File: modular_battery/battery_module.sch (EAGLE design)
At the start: 12 parts

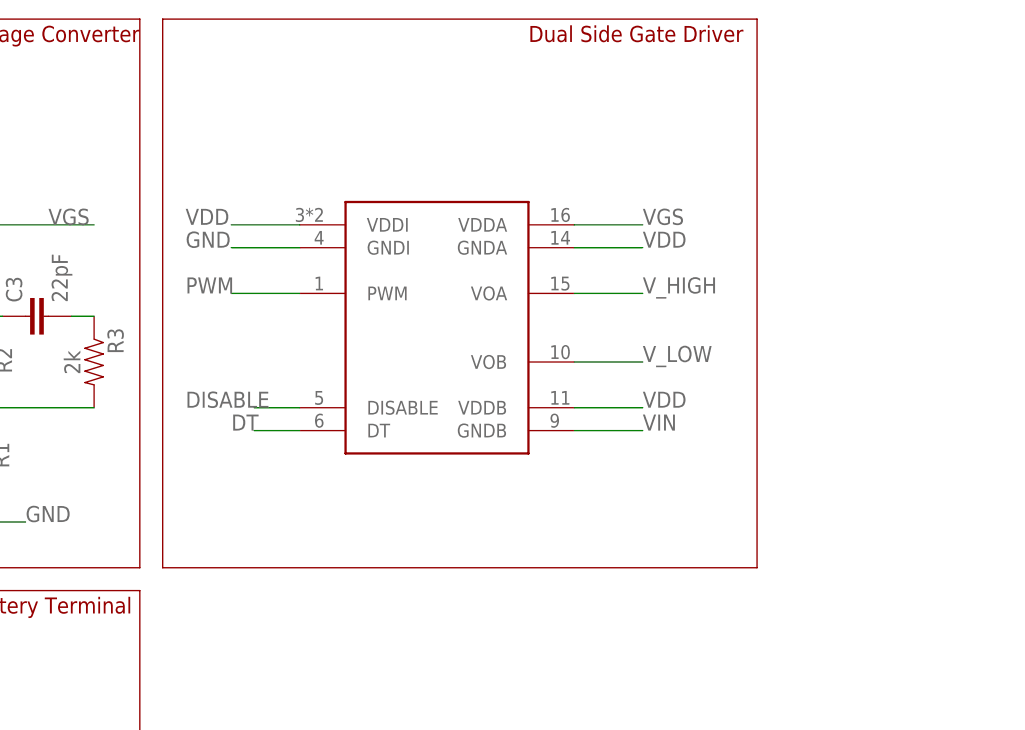
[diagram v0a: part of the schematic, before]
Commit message: Update battery_module.sch
Added bootstrap capacitor to high side mosfet driver.
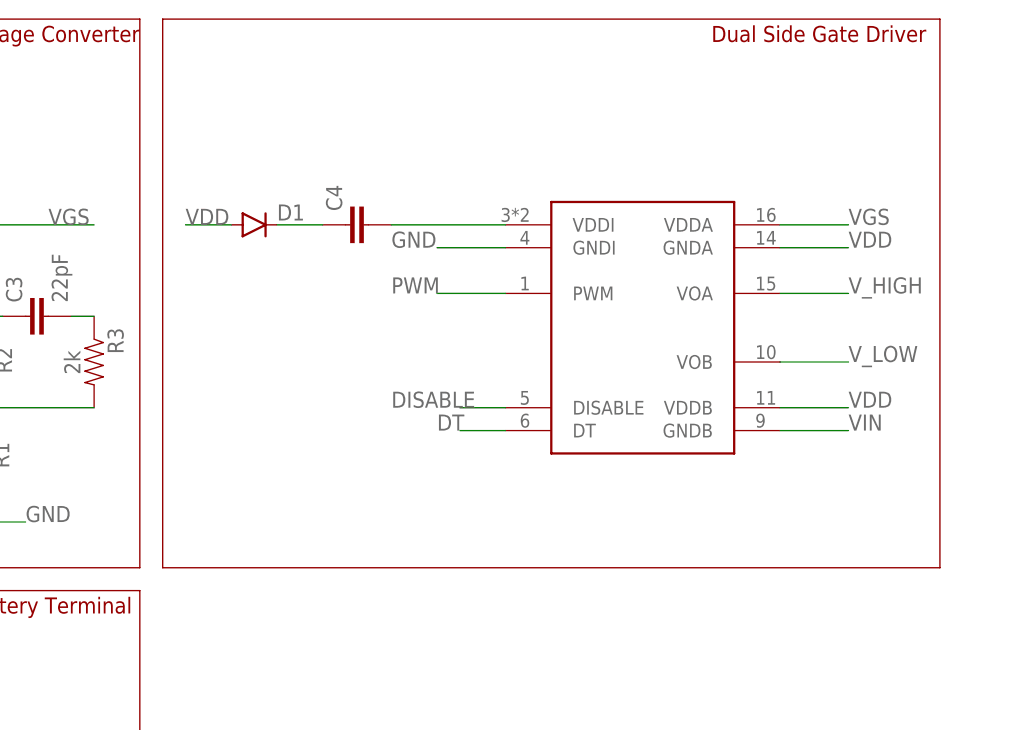
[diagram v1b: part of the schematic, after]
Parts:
- added C4: (no value), SparkFun-Passives:CAP0603-CAP
- added D1: (no value), SparkFun-DiscreteSemi:DIODESMB
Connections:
- new net N$2: C4.1, D1.C
- new net N$4: C4.2, U$4.VDDI
- net VDD: now also D1.A; no longer U$4.VDDI
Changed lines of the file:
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@@
 <part name="HIGH" library="IPT004N03L" deviceset="IPT004N03L" device=""/>
 <part name="L1" library="SparkFun-Passives" deviceset="INDUCTOR" device="30OHM,1.8A" value="22uH"/>
+<part name="C4" library="SparkFun-Passives" deviceset="CAP" device="0603-CAP"/>
+<part name="D1" library="SparkFun-DiscreteSemi" deviceset="DIODE" device="SMB"/>
 </parts>
 <sheets>
@@
 <wire x1="-25.4" y1="0" x2="-25.4" y2="43.18" width="0.1524" layer="94"/>
 <text x="12.7" y="40.64" size="1.778" layer="94">S1 Battery Terminal</text>
-<text x="78.74" y="104.14" size="1.778" layer="94">Dual Side Gate Driver</text>
-<wire x1="38.1" y1="106.68" x2="104.14" y2="106.68" width="0.1524" layer="94"/>
-<wire x1="104.14" y1="106.68" x2="104.14" y2="45.72" width="0.1524" layer="94"/>
-<wire x1="104.14" y1="45.72" x2="38.1" y2="45.72" width="0.1524" layer="94"/>
+<text x="99.06" y="104.14" size="1.778" layer="94">Dual Side Gate Driver</text>
+<wire x1="38.1" y1="106.68" x2="124.46" y2="106.68" width="0.1524" layer="94"/>
+<wire x1="124.46" y1="106.68" x2="124.46" y2="45.72" width="0.1524" layer="94"/>
+<wire x1="124.46" y1="45.72" x2="38.1" y2="45.72" width="0.1524" layer="94"/>
 <wire x1="38.1" y1="45.72" x2="38.1" y2="106.68" width="0.1524" layer="94"/>
 <text x="53.34" y="20.32" size="3.556" layer="94">LiPO Battery Module</text>
@@
 <instances>
 <instance part="U$3" gate="G$1" x="15.24" y="17.78"/>
-<instance part="U$4" gate="G$1" x="68.58" y="78.74"/>
+<instance part="U$4" gate="G$1" x="91.44" y="78.74"/>
 <instance part="LOW" gate="G$1" x="-2.54" y="12.7">
 <attribute name="NAME" x="-3.81" y="13.97" size="1.27" layer="95"/>
@@
 <attribute name="NAME" x="-17.78" y="73.66" size="1.778" layer="95" rot="R180"/>
 <attribute name="VALUE" x="-17.78" y="83.82" size="1.778" layer="96" rot="R180"/>
+</instance>
+<instance part="C4" gate="G$1" x="60.96" y="83.82" rot="R90">
+<attribute name="NAME" x="58.039" y="85.344" size="1.778" layer="95" rot="R90"/>
+<attribute name="VALUE" x="63.119" y="85.344" size="1.778" layer="96" rot="R90"/>
+</instance>
+<instance part="D1" gate="G$1" x="48.26" y="83.82">
+<attribute name="NAME" x="50.8" y="84.3026" size="1.778" layer="95"/>
+<attribute name="VALUE" x="50.8" y="81.5086" size="1.778" layer="96"/>
 </instance>
 </instances>
@@
 <segment>
 <pinref part="U$4" gate="G$1" pin="GNDI"/>
-<wire x1="53.34" y1="81.28" x2="45.72" y2="81.28" width="0.1524" layer="91"/>
-<label x="40.64" y="81.28" size="1.778" layer="95"/>
+<wire x1="76.2" y1="81.28" x2="68.58" y2="81.28" width="0.1524" layer="91"/>
+<label x="63.5" y="81.28" size="1.778" layer="95"/>
 </segment>
 </net>
@@
 <segment>
 <pinref part="U$4" gate="G$1" pin="VDDB"/>
-<wire x1="83.82" y1="63.5" x2="91.44" y2="63.5" width="0.1524" layer="91"/>
-<label x="91.44" y="63.5" size="1.778" layer="95"/>
+<wire x1="106.68" y1="63.5" x2="114.3" y2="63.5" width="0.1524" layer="91"/>
+<label x="114.3" y="63.5" size="1.778" layer="95"/>
 </segment>
 <segment>
 <pinref part="U$4" gate="G$1" pin="GNDA"/>
-<wire x1="83.82" y1="81.28" x2="91.44" y2="81.28" width="0.1524" layer="91"/>
-<label x="91.44" y="81.28" size="1.778" layer="95"/>
-</segment>
-<segment>
-<pinref part="U$4" gate="G$1" pin="VDDI"/>
-<wire x1="53.34" y1="83.82" x2="45.72" y2="83.82" width="0.1524" layer="91"/>
+<wire x1="106.68" y1="81.28" x2="114.3" y2="81.28" width="0.1524" layer="91"/>
+<label x="114.3" y="81.28" size="1.778" layer="95"/>
+</segment>
+<segment>
+<pinref part="D1" gate="G$1" pin="A"/>
+<wire x1="45.72" y1="83.82" x2="40.64" y2="83.82" width="0.1524" layer="91"/>
 <label x="40.64" y="83.82" size="1.778" layer="95"/>
 </segment>
@@
 <segment>
 <pinref part="U$4" gate="G$1" pin="VDDA"/>
-<wire x1="83.82" y1="83.82" x2="91.44" y2="83.82" width="0.1524" layer="91"/>
-<label x="91.44" y="83.82" size="1.778" layer="95"/>
+<wire x1="106.68" y1="83.82" x2="114.3" y2="83.82" width="0.1524" layer="91"/>
+<label x="114.3" y="83.82" size="1.778" layer="95"/>
 </segment>
 </net>
@@
 <segment>
 <pinref part="U$4" gate="G$1" pin="VOB"/>
-<wire x1="83.82" y1="68.58" x2="91.44" y2="68.58" width="0.1524" layer="91"/>
-<label x="91.44" y="68.58" size="1.778" layer="95"/>
+<wire x1="106.68" y1="68.58" x2="114.3" y2="68.58" width="0.1524" layer="91"/>
+<label x="114.3" y="68.58" size="1.778" layer="95"/>
 </segment>
 </net>
@@
 <segment>
 <pinref part="U$4" gate="G$1" pin="VOA"/>
-<wire x1="83.82" y1="76.2" x2="91.44" y2="76.2" width="0.1524" layer="91"/>
-<label x="91.44" y="76.2" size="1.778" layer="95"/>
+<wire x1="106.68" y1="76.2" x2="114.3" y2="76.2" width="0.1524" layer="91"/>
+<label x="114.3" y="76.2" size="1.778" layer="95"/>
 </segment>
 </net>
@@
 <segment>
 <pinref part="U$4" gate="G$1" pin="GNDB"/>
-<wire x1="83.82" y1="60.96" x2="91.44" y2="60.96" width="0.1524" layer="91"/>
-<label x="91.44" y="60.96" size="1.778" layer="95"/>
+<wire x1="106.68" y1="60.96" x2="114.3" y2="60.96" width="0.1524" layer="91"/>
+<label x="114.3" y="60.96" size="1.778" layer="95"/>
 </segment>
 </net>
@@
 <segment>
 <pinref part="U$4" gate="G$1" pin="PWM"/>
-<wire x1="53.34" y1="76.2" x2="45.72" y2="76.2" width="0.1524" layer="91"/>
-<label x="40.64" y="76.2" size="1.778" layer="95"/>
+<wire x1="76.2" y1="76.2" x2="68.58" y2="76.2" width="0.1524" layer="91"/>
+<label x="63.5" y="76.2" size="1.778" layer="95"/>
 </segment>
 </net>
@@
 <segment>
 <pinref part="U$4" gate="G$1" pin="DISABLE"/>
-<wire x1="53.34" y1="63.5" x2="48.26" y2="63.5" width="0.1524" layer="91"/>
-<label x="40.64" y="63.5" size="1.778" layer="95"/>
+<wire x1="76.2" y1="63.5" x2="71.12" y2="63.5" width="0.1524" layer="91"/>
+<label x="63.5" y="63.5" size="1.778" layer="95"/>
 </segment>
 </net>
@@
 <segment>
 <pinref part="U$4" gate="G$1" pin="DT"/>
-<wire x1="53.34" y1="60.96" x2="48.26" y2="60.96" width="0.1524" layer="91"/>
-<label x="45.72" y="60.96" size="1.778" layer="95"/>
-</segment>
-</net>
+<wire x1="76.2" y1="60.96" x2="71.12" y2="60.96" width="0.1524" layer="91"/>
+<label x="68.58" y="60.96" size="1.778" layer="95"/>
+</segment>
+</net>
+<net name="N$2" class="0">
+<segment>
+<pinref part="D1" gate="G$1" pin="C"/>
+<pinref part="C4" gate="G$1" pin="1"/>
+<wire x1="50.8" y1="83.82" x2="55.88" y2="83.82" width="0.1524" layer="91"/>
+</segment>
+</net>
+<net name="N$4" class="0">
+<segment>
+<pinref part="C4" gate="G$1" pin="2"/>
+<pinref part="U$4" gate="G$1" pin="VDDI"/>
+<wire x1="63.5" y1="83.82" x2="76.2" y2="83.82" width="0.1524" layer="91"/>
+</segment>
+</net>

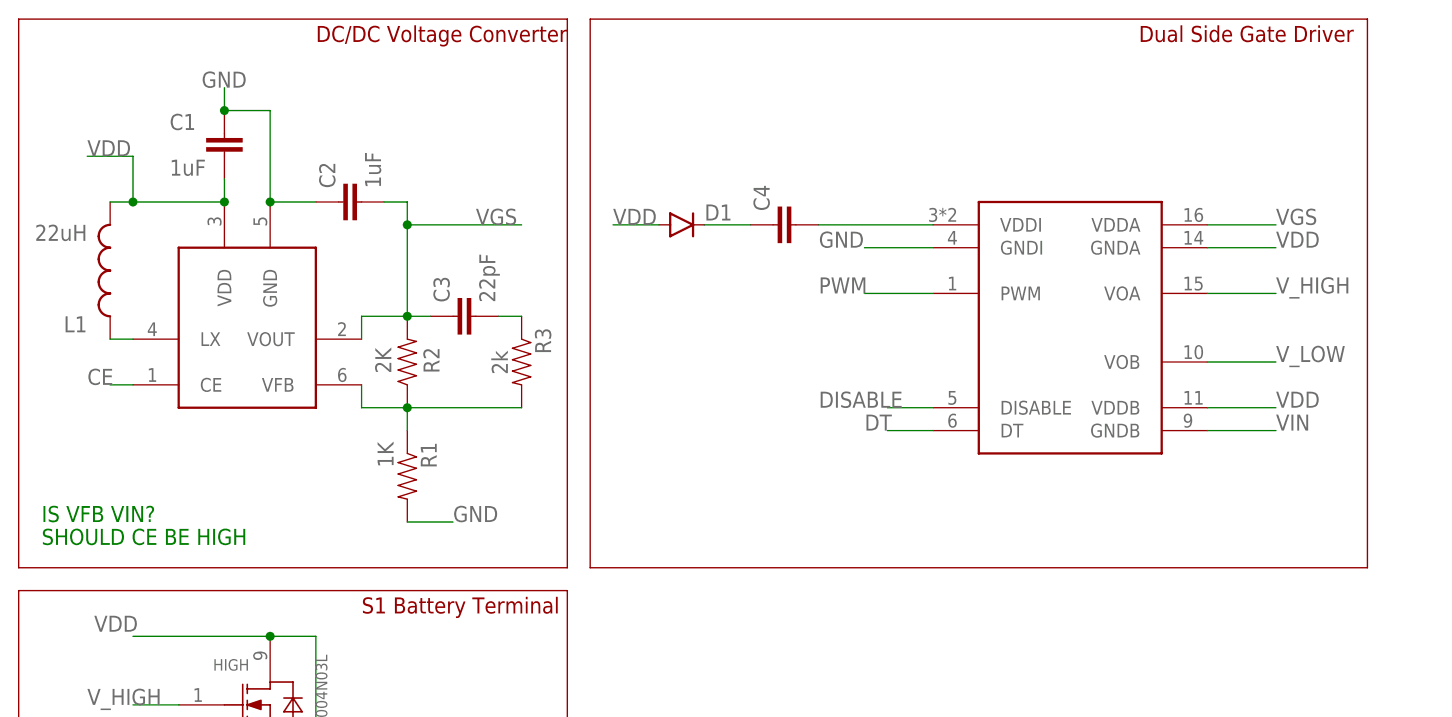
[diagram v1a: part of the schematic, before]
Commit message: boot strap and boost converter fixes
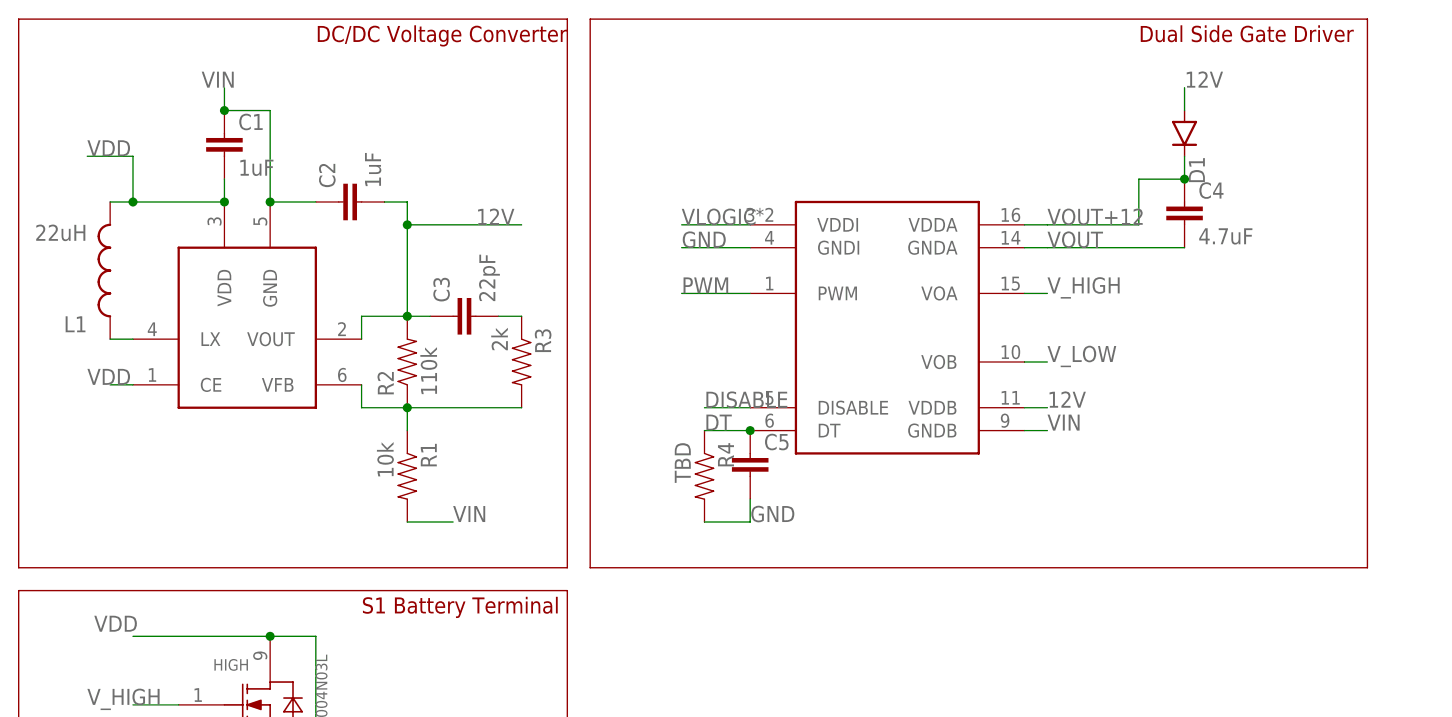
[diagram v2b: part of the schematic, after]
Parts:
- added C5: (no value), SparkFun-Passives:CAP0603-CAP
- added R4: TBD, SparkFun-Resistors:RESISTOR0603
- C4: value (none) -> 4.7uF
- R1: value 1K -> 10k
- R2: value 2K -> 110k
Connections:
- removed net CE: R1200.CE
- removed net N$2: C4.1, D1.C
- removed net N$4: C4.2, U$4.VDDI
- removed net VGS: C2.2, C3.1, R1200.VOUT, R2.2, U$4.VDDA
- new net 12V: C2.2, C3.1, D1.A, R1200.VOUT, R2.2, U$4.VDDB
- new net VLOGIC: U$4.VDDI
- new net VOUT+12: C4.1, D1.C, U$4.VDDA
- net DT: now also C5.1, R4.1
- net GND: now also C5.2, R4.2; no longer C1.1, C2.1, R1.2, R1200.GND
- net VDD: now also R1200.CE; no longer D1.A, U$4.GNDA, U$4.VDDB
- net VIN: now also C1.1, C2.1, R1.2, R1200.GND
- net VOUT: now also C4.2, U$4.GNDA
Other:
- note removed: "IS VFB VIN?"
- note removed: "SHOULD CE BE HIGH"
- moved on the sheet: C4, D1

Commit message: Layout for Modular Battery
Updated schematic for individual battery module and began layout for eight cell modular battery.
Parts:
- added ARRAY1: 47k, Custom_old:EXB-2HV
- added C10, C15, C20, C25, C30, C35, C40: (no value), SparkFun-Passives:CAP0603-CAP
- added C11, C13, C16, C18, C21, C23, C26, C28, C31, C33, C36, C38, C6, C8: 1uF, SparkFun-Capacitors:CAP0603-CAP
- added C12, C17, C22, C27, C32, C37, C7: 22pF, SparkFun-Capacitors:CAP0603-CAP
- added C14, C19, C24, C29, C34, C39, C9: 4.7uF, SparkFun-Passives:CAP0603-CAP
- added D2, D3, D4, D5, D6, D7, D8: (no value), SparkFun-DiscreteSemi:DIODESMB
- added HIGH1, HIGH2, HIGH3, HIGH4, HIGH5, HIGH6, HIGH7, LOW1, LOW2, LOW3, LOW4, LOW5, LOW6, LOW7: IPT004N03L, IPT004N03L:IPT004N03L
- added L2, L3, L4, L5, L6, L7, L8: (no value), PowerMagnetics (rev18e):WE-LQS_4025_74404043220A
- added R10, R15, R20, R25, R30, R35, R5: 10k, SparkFun-Resistors:RESISTOR0603
- added R11, R16, R21, R26, R31, R36, R6: 110k, SparkFun-Resistors:RESISTOR0603
- added R12, R17, R22, R27, R32, R37, R7: 2k, SparkFun-Resistors:RESISTOR0603
- added R13, R18, R23, R28, R33, R38, R8: R1200SOT-23-6, Custom_old:R1200SOT-23-6
- added R14, R19, R24, R29, R34, R39, R9: TBD, SparkFun-Resistors:RESISTOR0603
- added RC1_1, RC1_2, RC1_3, RC1_4, RC2_1, RC2_2, RC2_3, RC2_4: (no value), SparkFun-Capacitors:CAP1206
- added SI1, SI2, SI3, SI4, SI5, SI6, SI7, SI823: SI8231SOIC16W, Custom_old:SI8231SOIC16W
- added U$1, U$11: EXB-2HV, Custom_old:EXB-2HV
- added U$10, U$12: LM324, Custom_old:LM324
- added U$2, U$5, U$6, U$7, U$8, U$9: HEADER2, Custom_old:HEADER2
- L1: value 22uH -> (none); device SparkFun-Passives:INDUCTOR30OHM,1.8A -> PowerMagnetics (rev18e):WE-LQS_4025_74404043220A
- U$4: value SI8231SOIC16W -> HEADER2; device Custom_old:SI8231SOIC16W -> Custom_old:HEADER2
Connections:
- removed net 12V: C2.2, C3.1, D1.A, R1200.VOUT, R2.2, U$4.VDDB
- removed net DISABLE: U$4.DISABLE
- removed net DT: C5.1, R4.1, U$4.DT
- removed net PWM: U$4.PWM
- removed net VDD: C1.2, HIGH.9, L1.2, R1200.CE, R1200.VDD, U$3.1
- removed net VIN: C1.1, C2.1, LOW.2, LOW.3, LOW.4, LOW.5, LOW.6, LOW.7, LOW.8, R1.2, R1200.GND, U$3.2, U$4.GNDB
- removed net VOUT: C4.2, HIGH.2, HIGH.3, HIGH.4, HIGH.5, HIGH.6, HIGH.7, HIGH.8, LOW.9, U$4.GNDA
- removed net VOUT+12: C4.1, D1.C, U$4.VDDA
- removed net V_HIGH: HIGH.1, U$4.VOA
- removed net V_LOW: LOW.1, U$4.VOB
- new net 12V_A: C2.2, C3.1, D1.A, R1200.VOUT, R2.2, SI823.VDDB
- new net 12V_B: C7.1, C8.2, D2.A, R6.2, R8.VOUT, SI1.VDDB
- new net 12V_C: C12.1, C13.2, D3.A, R11.2, R13.VOUT, SI2.VDDB
- new net 12V_D: C17.1, C18.2, D4.A, R16.2, R18.VOUT, SI3.VDDB
- new net 12V_E: C22.1, C23.2, D5.A, R21.2, R23.VOUT, SI4.VDDB
- new net 12V_F: C27.1, C28.2, D6.A, R26.2, R28.VOUT, SI5.VDDB
- new net 12V_G: C32.1, C33.2, D7.A, R31.2, R33.VOUT, SI6.VDDB
- new net 12V_H: C37.1, C38.2, D8.A, R36.2, R38.VOUT, SI7.VDDB
- new net DISABLE_A: SI823.DISABLE
- new net DISABLE_B: SI1.DISABLE
- new net DISABLE_C: SI2.DISABLE
- new net DISABLE_D: SI3.DISABLE
- new net DISABLE_E: SI4.DISABLE
- new net DISABLE_F: SI5.DISABLE
- new net DISABLE_G: SI6.DISABLE
- new net DISABLE_H: SI7.DISABLE
- new net DT_A: C5.1, R4.1, SI823.DT
- new net DT_B: C10.1, R9.1, SI1.DT
- new net DT_C: C15.1, R14.1, SI2.DT
- new net DT_D: C20.1, R19.1, SI3.DT
- new net DT_E: C25.1, R24.1, SI4.DT
- new net DT_F: C30.1, R29.1, SI5.DT
- new net DT_G: C35.1, R34.1, SI6.DT
- new net DT_H: C40.1, R39.1, SI7.DT
- new net N$10: R15.1, R16.1, R17.2, R18.VFB
- new net N$11: L4.1, R18.LX
- new net N$12: C17.2, R17.1
- new net N$13: R20.1, R21.1, R22.2, R23.VFB
- new net N$14: L5.1, R23.LX
- new net N$15: C22.2, R22.1
- new net N$16: R25.1, R26.1, R27.2, R28.VFB
- new net N$17: L6.1, R28.LX
- new net N$18: C27.2, R27.1
- new net N$19: R30.1, R31.1, R32.2, R33.VFB
- new net N$2: R5.1, R6.1, R7.2, R8.VFB
- new net N$20: L7.1, R33.LX
- new net N$21: C32.2, R32.1
- new net N$22: R35.1, R36.1, R37.2, R38.VFB
- new net N$23: L8.1, R38.LX
- new net N$24: C37.2, R37.1
- new net N$4: L2.1, R8.LX
- new net N$6: C7.2, R7.1
- new net N$7: R10.1, R11.1, R12.2, R13.VFB
- new net N$8: L3.1, R13.LX
- new net N$9: C12.2, R12.1
- new net PWM_A: SI823.PWM
- new net PWM_B: SI1.PWM
- new net PWM_C: SI2.PWM
- new net PWM_D: SI3.PWM
- new net PWM_E: SI4.PWM
- new net PWM_F: SI5.PWM
- new net PWM_G: SI6.PWM
- new net PWM_H: SI7.PWM
- new net VDD_A: ARRAY1.P$1, C1.2, HIGH.9, L1.2, R1200.CE, R1200.VDD, U$3.1
- new net VDD_B: ARRAY1.P$2, C6.2, HIGH1.9, L2.2, R8.CE, R8.VDD, U$2.1
- new net VDD_C: ARRAY1.P$3, C11.2, HIGH2.9, L3.2, R13.CE, R13.VDD, U$4.1
- new net VDD_D: ARRAY1.P$4, C16.2, HIGH3.9, L4.2, R18.CE, R18.VDD, U$5.1
- new net VDD_E: ARRAY1.P$5, C21.2, HIGH4.9, L5.2, R23.CE, R23.VDD, U$6.1
- new net VDD_F: ARRAY1.P$6, C26.2, HIGH5.9, L6.2, R28.CE, R28.VDD, U$7.1
- new net VDD_G: ARRAY1.P$7, C31.2, HIGH6.9, L7.2, R33.CE, R33.VDD, U$8.1
- new net VDD_H: ARRAY1.P$8, C36.2, HIGH7.9, L8.2, R38.CE, R38.VDD, U$9.1
- new net VDIVRC_A: RC1_1.1, U$11.P$16, U$12.1IN+
- new net VDIVRC_B: RC1_2.1, U$11.P$15, U$12.2IN+
- new net VDIVRC_C: RC1_3.1, U$11.P$14, U$12.3IN+
- new net VDIVRC_D: RC1_4.1, U$11.P$13, U$12.4IN+
- new net VDIVRC_E: RC2_1.1, U$10.1IN+, U$10.2IN+, U$11.P$12
- new net VDIVRC_F: RC2_2.1, U$11.P$11
- new net VDIVRC_G: RC2_3.1, U$10.3IN+, U$11.P$10
- new net VDIVRC_H: RC2_4.1, U$10.4IN+, U$11.P$9
- new net VDIV_A: ARRAY1.P$16, U$1.P$1, U$11.P$1
- new net VDIV_B: ARRAY1.P$15, U$1.P$2, U$11.P$2
- new net VDIV_C: ARRAY1.P$14, U$1.P$3, U$11.P$3
- new net VDIV_D: ARRAY1.P$13, U$1.P$4, U$11.P$4
- new net VDIV_E: ARRAY1.P$12, U$1.P$5, U$11.P$5
- new net VDIV_F: ARRAY1.P$11, U$1.P$6, U$11.P$6
- new net VDIV_G: ARRAY1.P$10, U$1.P$7, U$11.P$7
- new net VDIV_H: ARRAY1.P$9, U$1.P$8, U$11.P$8
- new net VIN_A: C1.1, C2.1, LOW.2, LOW.3, LOW.4, LOW.5, LOW.6, LOW.7, LOW.8, R1.2, R1200.GND, SI823.GNDB, U$3.2
- new net VOUT+12_A: C4.1, D1.C, SI823.VDDA
- new net VOUT+12_B: C9.1, D2.C, SI1.VDDA
- new net VOUT+12_C: C14.1, D3.C, SI2.VDDA
- new net VOUT+12_D: C19.1, D4.C, SI3.VDDA
- new net VOUT+12_E: C24.1, D5.C, SI4.VDDA
- new net VOUT+12_F: C29.1, D6.C, SI5.VDDA
- new net VOUT+12_G: C34.1, D7.C, SI6.VDDA
- new net VOUT+12_H: C39.1, D8.C, SI7.VDDA
- new net VOUT_A: C4.2, C6.1, C8.1, HIGH.2, HIGH.3, HIGH.4, HIGH.5, HIGH.6, HIGH.7, HIGH.8, LOW.9, LOW1.2, LOW1.3, LOW1.4, LOW1.5, LOW1.6, LOW1.7, LOW1.8, R5.2, R8.GND, SI1.GNDB, SI823.GNDA, U$2.2
- new net VOUT_B: C11.1, C13.1, C9.2, HIGH1.2, HIGH1.3, HIGH1.4, HIGH1.5, HIGH1.6, HIGH1.7, HIGH1.8, LOW1.9, LOW2.2, LOW2.3, LOW2.4, LOW2.5, LOW2.6, LOW2.7, LOW2.8, R10.2, R13.GND, SI1.GNDA, SI2.GNDB, U$4.2
- new net VOUT_C: C14.2, C16.1, C18.1, HIGH2.2, HIGH2.3, HIGH2.4, HIGH2.5, HIGH2.6, HIGH2.7, HIGH2.8, LOW2.9, LOW3.2, LOW3.3, LOW3.4, LOW3.5, LOW3.6, LOW3.7, LOW3.8, R15.2, R18.GND, SI2.GNDA, SI3.GNDB, U$5.2
- new net VOUT_D: C19.2, C21.1, C23.1, HIGH3.2, HIGH3.3, HIGH3.4, HIGH3.5, HIGH3.6, HIGH3.7, HIGH3.8, LOW3.9, LOW4.2, LOW4.3, LOW4.4, LOW4.5, LOW4.6, LOW4.7, LOW4.8, R20.2, R23.GND, SI3.GNDA, SI4.GNDB, U$6.2
- new net VOUT_E: C24.2, C26.1, C28.1, HIGH4.2, HIGH4.3, HIGH4.4, HIGH4.5, HIGH4.6, HIGH4.7, HIGH4.8, LOW4.9, LOW5.2, LOW5.3, LOW5.4, LOW5.5, LOW5.6, LOW5.7, LOW5.8, R25.2, R28.GND, SI4.GNDA, SI5.GNDB, U$7.2
- new net VOUT_F: C29.2, C31.1, C33.1, HIGH5.2, HIGH5.3, HIGH5.4, HIGH5.5, HIGH5.6, HIGH5.7, HIGH5.8, LOW5.9, LOW6.2, LOW6.3, LOW6.4, LOW6.5, LOW6.6, LOW6.7, LOW6.8, R30.2, R33.GND, SI5.GNDA, SI6.GNDB, U$8.2
- new net VOUT_G: C34.2, C36.1, C38.1, HIGH6.2, HIGH6.3, HIGH6.4, HIGH6.5, HIGH6.6, HIGH6.7, HIGH6.8, LOW6.9, LOW7.2, LOW7.3, LOW7.4, LOW7.5, LOW7.6, LOW7.7, LOW7.8, R35.2, R38.GND, SI6.GNDA, SI7.GNDB, U$9.2
- new net VOUT_H: C39.2, HIGH7.2, HIGH7.3, HIGH7.4, HIGH7.5, HIGH7.6, HIGH7.7, HIGH7.8, LOW7.9, SI7.GNDA
- new net VSENSE_A: U$12.1IN-, U$12.1OUT
- new net VSENSE_B: U$12.2IN-, U$12.2OUT
- new net VSENSE_C: U$12.3IN-, U$12.3OUT
- new net VSENSE_D: U$12.4IN-, U$12.4OUT
- new net VSENSE_E: U$10.1IN-, U$10.1OUT
- new net VSENSE_F: U$10.2IN-, U$10.2OUT
- new net VSENSE_G: U$10.3IN-, U$10.3OUT
- new net VSENSE_H: U$10.4IN-, U$10.4OUT
- new net V_HIGH_A: HIGH.1, SI823.VOA
- new net V_HIGH_B: HIGH1.1, SI1.VOA
- new net V_HIGH_C: HIGH2.1, SI2.VOA
- new net V_HIGH_D: HIGH3.1, SI3.VOA
- new net V_HIGH_E: HIGH4.1, SI4.VOA
- new net V_HIGH_F: HIGH5.1, SI5.VOA
- new net V_HIGH_G: HIGH6.1, SI6.VOA
- new net V_HIGH_H: HIGH7.1, SI7.VOA
- new net V_LOW_A: LOW.1, SI823.VOB
- new net V_LOW_B: LOW1.1, SI1.VOB
- new net V_LOW_C: LOW2.1, SI2.VOB
- new net V_LOW_D: LOW3.1, SI3.VOB
- new net V_LOW_E: LOW4.1, SI4.VOB
- new net V_LOW_F: LOW5.1, SI5.VOB
- new net V_LOW_G: LOW6.1, SI6.VOB
- new net V_LOW_H: LOW7.1, SI7.VOB
- net GND: now also C10.2, C15.2, C20.2, C25.2, C30.2, C35.2, C40.2, R14.2, R19.2, R24.2, R29.2, R34.2, R39.2, R9.2, RC1_1.2, RC1_2.2, RC1_3.2, RC1_4.2, RC2_1.2, RC2_2.2, RC2_3.2, RC2_4.2, SI1.GNDI, SI2.GNDI, SI3.GNDI, SI4.GNDI, SI5.GNDI, SI6.GNDI, SI7.GNDI, SI823.GNDI, U$1.P$10, U$1.P$11, U$1.P$12, U$1.P$13, U$1.P$14, U$1.P$15, U$1.P$16, U$1.P$9, U$10.GND, U$12.GND; no longer U$4.GNDI
- net VLOGIC: now also SI1.VDDI, SI2.VDDI, SI3.VDDI, SI4.VDDI, SI5.VDDI, SI6.VDDI, SI7.VDDI, SI823.VDDI, U$10.VCC, U$12.VCC; no longer U$4.VDDI
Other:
- note added: "A"
- note added: "B"
- note added: "C"
- note added: "D"
- note added: "E"
- note added: "F"
- note added: "G"
- note added: "H"
- note added: "Op Amp Array"
- note added: "RC Filter"
- note added: "Voltage Divider Array"
- moved on the sheet: C1, C2, C3, C4, C5, D1, HIGH, LOW, R1, R2, R3, R4
